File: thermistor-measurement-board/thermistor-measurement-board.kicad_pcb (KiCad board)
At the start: 4 copper layers, 50.8 x 30.5 mm, 94 parts, among them P201 BIAS, P301 MEASURE, P401 PWR, P402 BIAS, P403 OUT_A, P404 OUT_B, P406 I/O, U201 MAX14661, U202 AD8607, U203 AD8277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

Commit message: some schematic review and a new TODO list
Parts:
- R301, R302: value R -> 660k
- R311, R312: value 0 -> 100k
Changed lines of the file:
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@@
     (links 287)
     (no_connects 0)
-    (area 156.794287 61.92 221.680798 101.93528)
+    (area 168.834999 69.774999 219.785001 100.405001)
     (thickness 1.6)
     (drawings 16)
@@
       (effects (font (size 0.508 0.508) (thickness 0.0762)))
     )
-    (fp_text value R (at 0 0.097102 270) (layer F.Fab)
+    (fp_text value 660k (at 0 0.097102 270) (layer F.Fab)
       (effects (font (size 0.508 0.508) (thickness 0.0762)))
     )
@@
       (effects (font (size 0.508 0.508) (thickness 0.0762)))
     )
-    (fp_text value R (at 0 0.097102 270) (layer F.Fab)
+    (fp_text value 660k (at 0 0.097102 270) (layer F.Fab)
       (effects (font (size 0.508 0.508) (thickness 0.0762)))
     )
@@
       (effects (font (size 0.508 0.508) (thickness 0.0762)))
     )
-    (fp_text value 0 (at 0 0.032742) (layer F.Fab)
+    (fp_text value 100k (at 0 0.032742) (layer F.Fab)
       (effects (font (size 0.508 0.508) (thickness 0.0762)))
     )
@@
       (effects (font (size 0.508 0.508) (thickness 0.0762)))
     )
-    (fp_text value 0 (at 0 0.179742) (layer F.Fab)
-      (effects (font (size 0.508 0.508) (thickness 0.0762)))
-    )
+    (fp_text value 100k (at 0 0.179742) (layer F.Fab)
+      (effects (font (size 0.508 0.508) (thickness 0.0762)))
+    )

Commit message: took care of a few board review tasks
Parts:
- added C322: 0.1u, Capacitors_SMD:C_0402, F.Cu at (188.8, 85.8)
- added P405: ADC_REF, Pin_Headers:Pin_Header_Straight_1x02, F.Cu at (175.3, 71.1)
- added R211: 100k, Resistors_SMD:R_0402, F.Cu at (216.1, 91.9)
- added R212: 100k, Resistors_SMD:R_0402, F.Cu at (210.4, 91.8)
- added R324: 0, Resistors_SMD:R_0603, F.Cu at (189.1, 87.4)
- R301, R302: value 660k -> 6.6M
- R311, R312: value 100k -> 1M
- moved C317 1.37 mm to (188.0, 87.1), turned to 270 degrees
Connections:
- net Net-(C317-Pad1) renamed /Interface/ADC_REF+
- U304 pad 3: /Interface/OUT_B+ -> /Interface/OUT_B-
- U304 pad 4: /Interface/OUT_B- -> /Interface/OUT_B+
- U304 pad 7: GNDA -> /Interface/ADC_REF-
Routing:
- net /Interface/ADC_REF-: track 0.00 -> 25.8 mm, vias 0 -> 1
- net /Interface/ADC_REF+: track 1.56 -> 23.4 mm, vias 0 -> 1
- net /Bias/VREF2_EN: track 13.4 -> 20.5 mm
- net GNDA: track 110.6 -> 114.5 mm, vias 43 -> 46
- net /Bias/VREF1_EN: track 10.7 -> 11.4 mm
- net GND: track 40.7 -> 40.0 mm
- net /Bias/AVCC: track 36.2 -> 36.4 mm, vias 18 -> 17
- net /Interface/OUT_B+: vias 1 -> 3
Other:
- rule trace_min: 0.127 -> 0.1524

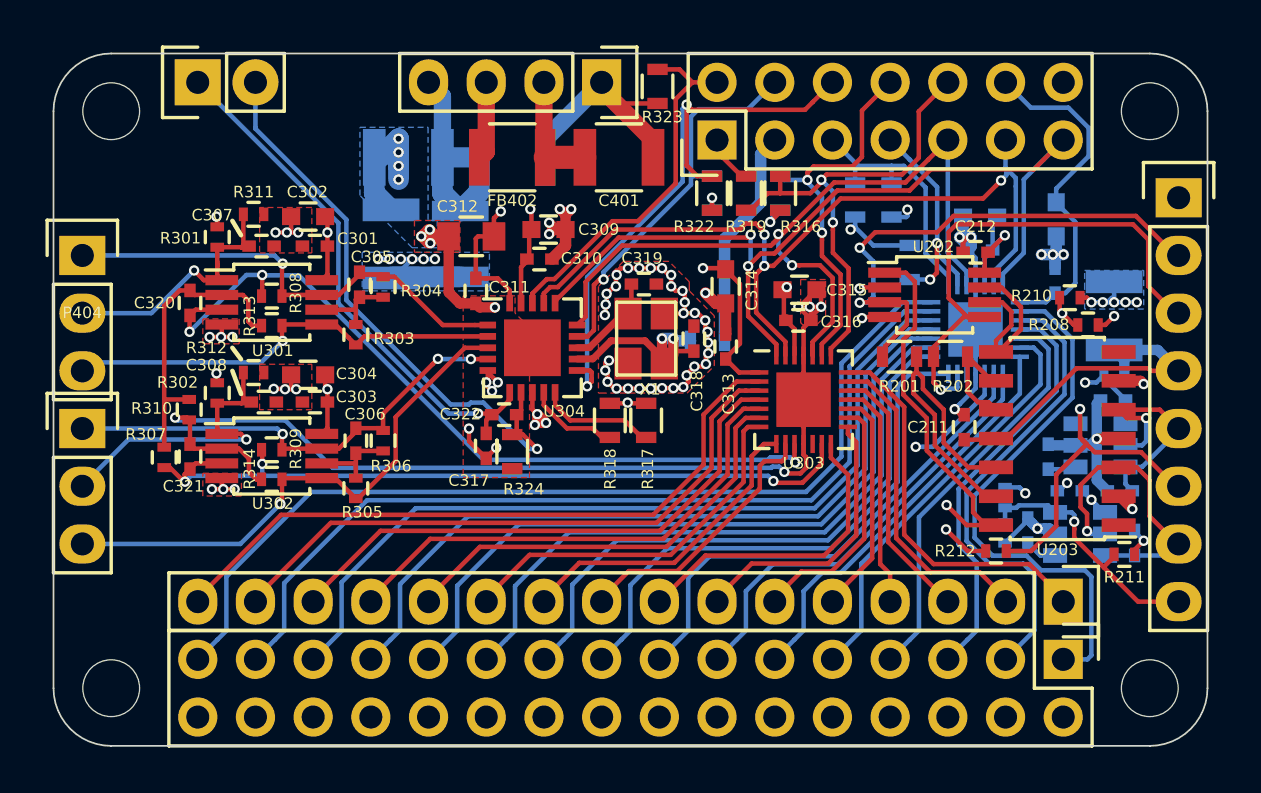
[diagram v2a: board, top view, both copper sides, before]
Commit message: reviewed footprints
they were all more or less correct, but i massaged a couple to closer match Maxim's recommended land patterns
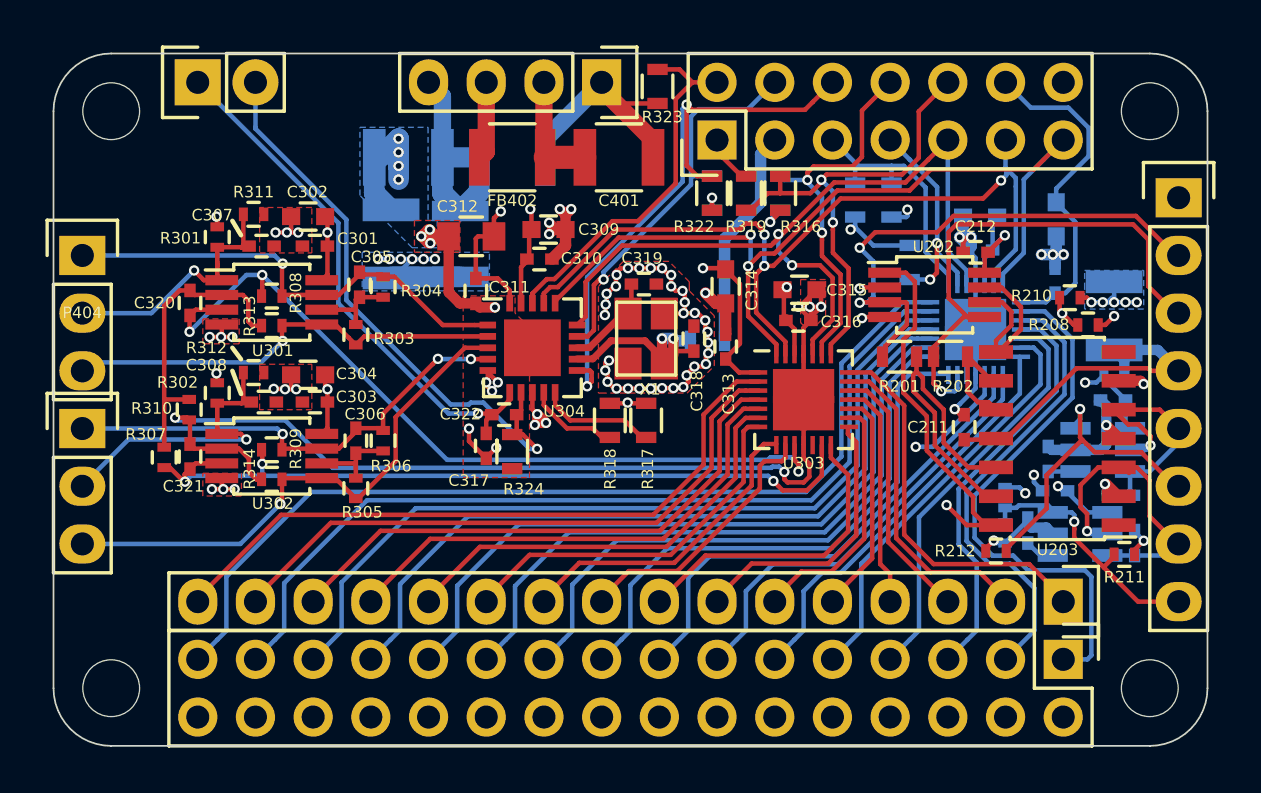
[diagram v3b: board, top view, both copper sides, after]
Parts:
- U201, U303: footprint Housings_DFN_QFN:QFN-28-1EP_4x4mm_Pitch0.4mm -> project:Maxim_90-0035
- U204, U205: footprint TO_SOT_Packages_SMD:SOT-23-6 -> project:Maxim_90-0175
- moved C207 0.65 mm to (213.0, 89.1)
- moved U205 0.22 mm to (215.1, 87.3)
- moved C206 0.21 mm to (215.9, 89.3)
- moved C210 0.10 mm to (212.7, 87.7)
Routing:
- net /Bias/AVCC: track 36.4 -> 37.8 mm
- net /Measurement/COM_A: track 35.3 -> 36.2 mm
- net /Bias/VREF2_EN: track 20.5 -> 19.7 mm
- net /Measurement/COM_B: track 34.0 -> 34.6 mm
- net GNDA: track 114.5 -> 113.9 mm, vias 46 -> 45
- net /Bias/SCLK: track 35.7 -> 35.2 mm

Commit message: some notes and minor fiddling around
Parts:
- R201, R202: value R -> 0.01%
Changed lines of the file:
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@@
     (links 296)
     (no_connects 0)
-    (area 168.871899 69.811899 219.748101 100.368101)
+    (area 156.794287 61.92 221.680798 101.93528)
     (thickness 1.6)
     (drawings 15)
@@
       (effects (font (size 0.508 0.508) (thickness 0.0762)))
     )
-    (fp_text value R (at -0.058 -0.036 180) (layer F.Fab)
+    (fp_text value 0.01% (at -0.058 -0.036 180) (layer F.Fab)
       (effects (font (size 0.508 0.508) (thickness 0.0762)))
     )
@@
       (effects (font (size 0.508 0.508) (thickness 0.0762)))
     )
-    (fp_text value R (at 0 -0.012 180) (layer F.Fab)
-      (effects (font (size 0.508 0.508) (thickness 0.0762)))
-    )
+    (fp_text value 0.01% (at 0 -0.012 180) (layer F.Fab)
+      (effects (font (size 0.508 0.508) (thickness 0.0762)))
+    )

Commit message: lots of design review and related fixes/improvements
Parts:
- added C323: 100p, Capacitors_SMD:C_0402, F.Cu at (186.6, 82.3)
- added C324: 100p, Capacitors_SMD:C_0402, F.Cu at (186.6, 84.4)
- added D301: 1.8V, Diodes_SMD:SOD-123, B.Cu at (174.4, 86.4)
- added D302: 1.8V, Diodes_SMD:SOD-123, B.Cu at (174.4, 78.7)
- added D303: 1.8V, Diodes_SMD:SOD-123, B.Cu at (174.4, 91.4)
- added D304: 1.8V, Diodes_SMD:SOD-123, B.Cu at (174.4, 83.8)
- added R325: 0, Resistors_SMD:R_0603, F.Cu at (185.0, 86.1)
- added R326: 0, Resistors_SMD:R_0603, F.Cu at (185.6, 84.4)
- C322: value 0.1u -> 100p
- P405: footprint Pin_Headers:Pin_Header_Straight_1x02 -> Pin_Headers:Pin_Header_Straight_1x04
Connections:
- P405 pad 2: /Interface/ADC_REF- -> /Interface/ADC_REF+
- U304 pad 3: /Interface/OUT_B- -> Net-(C324-Pad1)
- U304 pad 4: /Interface/OUT_B+ -> Net-(C324-Pad2)
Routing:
- net /Interface/ADC_REF+: track 23.4 -> 50.0 mm, vias 1 -> 2
- net /Interface/ADC_REF-: track 25.8 -> 46.9 mm, vias 1 -> 2
- net /Interface/OUT_B+: track 21.1 -> 16.6 mm, vias 3 -> 1
- net Net-(C324-Pad2): track 0.00 -> 4.01 mm
- net /Interface/OUT_B-: track 23.9 -> 20.1 mm
- net Net-(C324-Pad1): track 0.00 -> 2.94 mm
- net GNDA: track 113.9 -> 115.3 mm, vias 45 -> 47
- net /Interface/OUT_A+: track 20.9 -> 21.7 mm
- net /Measurement/COM_A: track 36.2 -> 36.9 mm

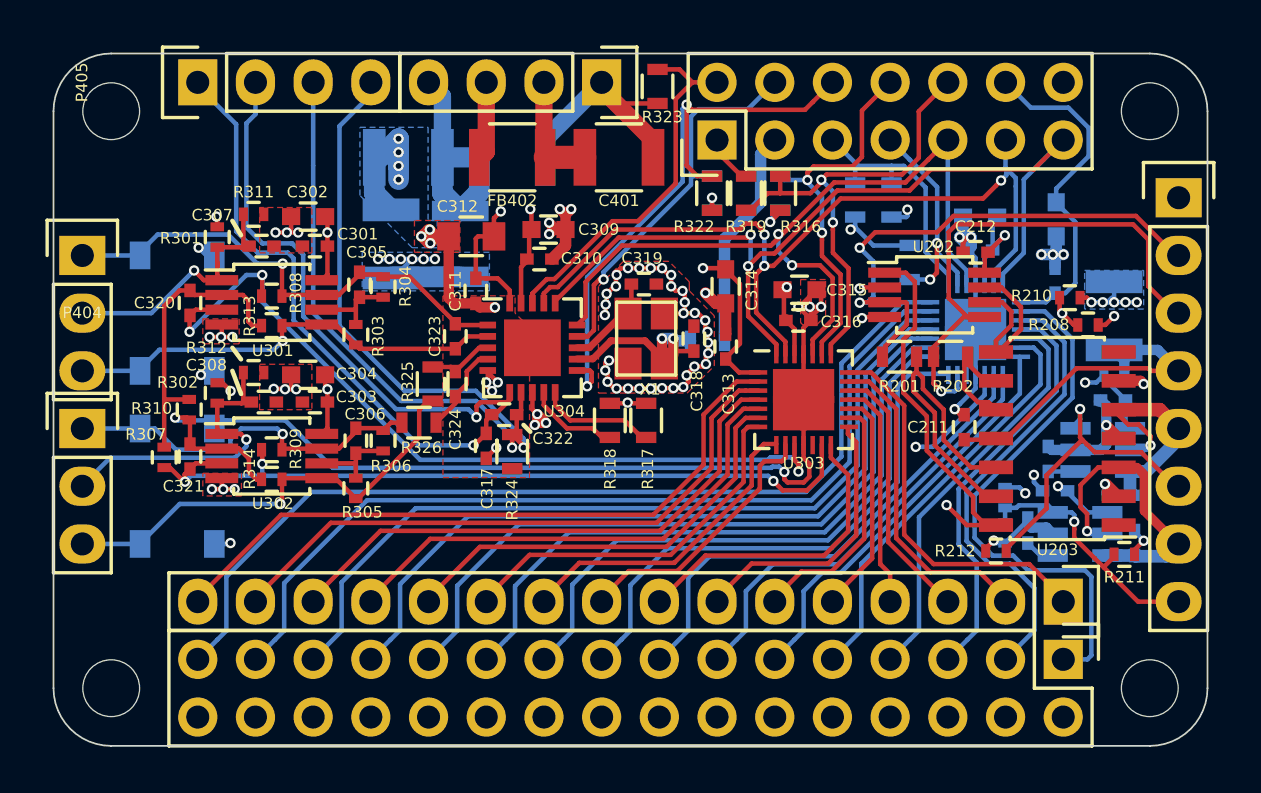
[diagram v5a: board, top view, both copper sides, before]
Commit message: read a million instrument amp datasheets and found one that should work nicely for low gain.
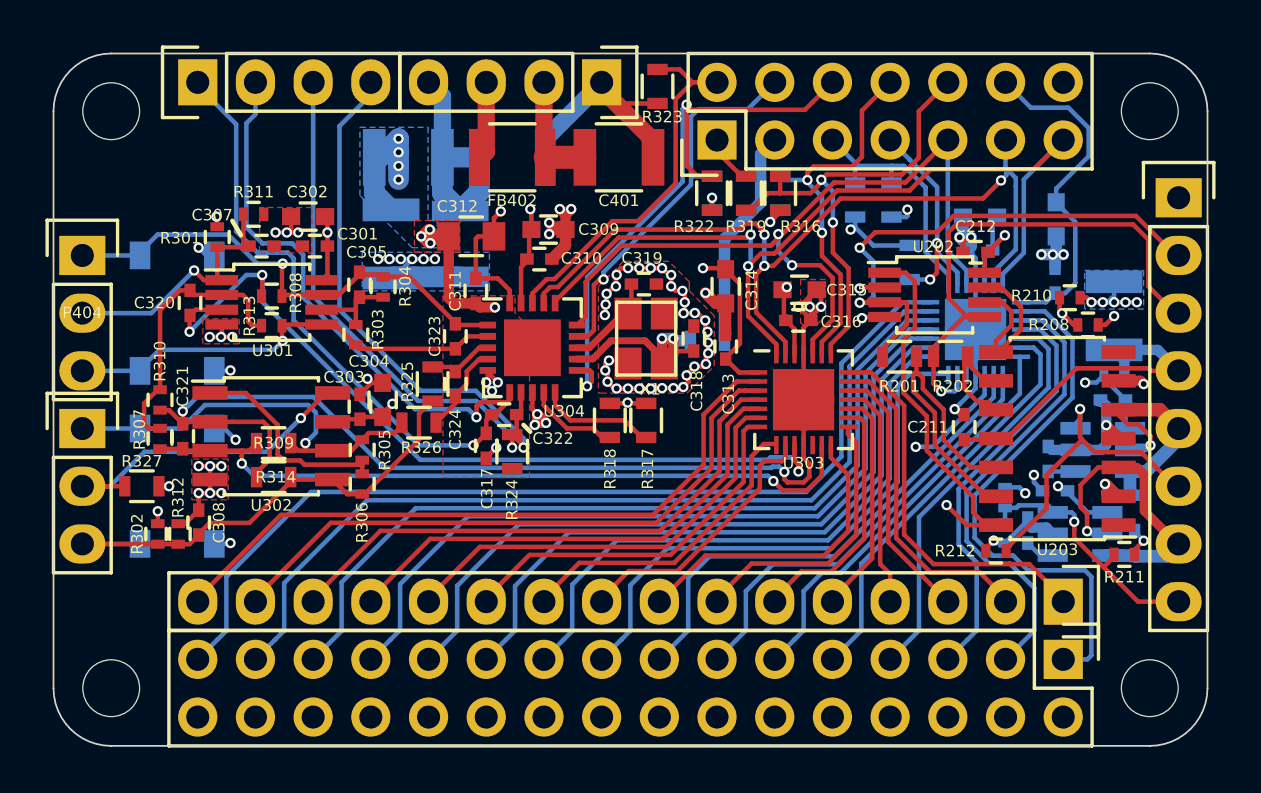
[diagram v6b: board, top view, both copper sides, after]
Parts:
- removed C306: 0.01u, Capacitors_SMD:C_0402
- removed REF** (x4): MountingHole_2-5mm, Mounting_Holes:MountingHole_2-5mm
- added H401: MountingHole, MountingHole_2-5mm, F.Cu at (171.4, 72.4)
- added H402: MountingHole, MountingHole_2-5mm, F.Cu at (217.2, 72.4)
- added H403: MountingHole, MountingHole_2-5mm, F.Cu at (171.4, 97.8)
- added H404: MountingHole, MountingHole_2-5mm, F.Cu at (217.2, 97.8)
- added R327: 100k, Resistors_SMD:R_0603, F.Cu at (172.8, 88.9)
- R301, R302: value 6.6M -> 7.5M
- R304: value 0 -> 63k
- R305: value 1k -> 0
- R306: value 99k -> ∞
- R309, R314: footprint Resistors_SMD:R_0402 -> Resistors_SMD:R_0603
- R311, R312: value 1M -> 2.5M
- U301: value MAX4208 -> MAX4209
- U302: value MAX4209 -> MCP6N11; footprint Housings_SSOP:MSOP-8_3x3mm_Pitch0.65mm -> Housings_SOIC:SOIC-8_3.9x4.9mm_Pitch1.27mm
- moved R312 7.84 mm to (174.4, 91.0), turned to 90 degrees
- moved R302 6.74 mm to (173.5, 91.0)
- moved C308 6.03 mm to (175.3, 90.5), turned to 90 degrees
- moved C304 3.46 mm to (183.4, 85.1), turned to 90 degrees
- moved R306 2.12 mm to (182.5, 88.8), turned to 270 degrees
- moved C303 1.99 mm to (182.4, 85.4), turned to 90 degrees
- moved R305 1.72 mm to (182.5, 87.3), turned to 90 degrees
- moved R310 1.35 mm to (173.6, 85.1)
- moved C321 0.95 mm to (174.6, 86.7)
- moved U302 0.87 mm to (178.5, 86.7)
- moved R307 0.85 mm to (173.6, 86.8)
- moved R309 0.31 mm to (178.6, 87.0)
- moved R314 0.12 mm to (178.6, 88.5)
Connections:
- net /Bias/DVDD renamed /ADC/DVDD
- net /Bias/MISO renamed /ADC/MISO
- net /Bias/MOSI renamed /ADC/MOSI
- net /Bias/SCLK renamed /ADC/SCLK
- net /Interface/ADC_CS renamed /ADC/ADC_CS
- net /Interface/ADC_DR_INT renamed /ADC/ADC_DR_INT
- net /Interface/ADC_MCLK renamed /ADC/ADC_MCLK
- net /Interface/ADC_REF+ renamed /ADC/ADC_REF+
- net /Interface/ADC_REF- renamed /ADC/ADC_REF-
- net /Interface/ADC_RST renamed /ADC/ADC_RST
- net /Interface/OUT_A+ renamed /ADC/OUT_A+
- net /Interface/OUT_A- renamed /ADC/OUT_A-
- net /Measurement/ADC_OSC1 renamed /ADC/ADC_OSC1
- net /Measurement/ADC_OSC2 renamed /ADC/ADC_OSC2
- net /Measurement/COM_A renamed /Sensor input/COM_A
- net /Measurement/COM_B renamed /Sensor input/COM_B
- net Net-(C320-Pad2) renamed /Sensor input/IN_A-
- C201 pad 1: /Bias/AVCC -> /ADC/AVCC
- C202 pad 1: /Bias/AVCC -> /ADC/AVCC
- C207 pad 1: /Bias/AVCC -> /ADC/AVCC
- C209 pad 1: /Bias/AVCC -> /ADC/AVCC
- C212 pad 1: /Bias/AVCC -> /ADC/AVCC
- C301 pad 1: /Bias/AVCC -> /ADC/AVCC
- C302 pad 1: /Bias/AVCC -> /ADC/AVCC
- C303 pad 1: /Bias/AVCC -> /ADC/AVCC
- C304 pad 1: /Bias/AVCC -> /ADC/AVCC
- C308 pad 1: /Interface/REF_B -> /ADC/OUT_B-
- C311 pad 1: /Bias/AVCC -> /ADC/AVCC
- C312 pad 1: /Bias/AVCC -> /ADC/AVCC
- C315 pad 1: /Bias/AVCC -> /ADC/AVCC
- C316 pad 1: /Bias/AVCC -> /ADC/AVCC
- C403 pad 1: /Bias/AVCC -> /ADC/AVCC
- D301 pad 1: /Interface/OUT_B+ -> /ADC/OUT_B+
- D303 pad 1: /Interface/OUT_B- -> /ADC/OUT_B-
- P404 pad 1: /Interface/OUT_B+ -> /ADC/OUT_B+
- P404 pad 2: /Interface/REF_B -> /Sensor input/AMP_B_EN
- P404 pad 3: /Interface/OUT_B- -> /ADC/OUT_B-
- R206 pad 2: /Bias/AVCC -> /ADC/AVCC
- R207 pad 2: /Bias/AVCC -> /ADC/AVCC
- R208 pad 2: /Bias/AVCC -> /ADC/AVCC
- R301 pad 1: /Bias/AVCC -> /ADC/AVCC
- R302 pad 1: /Bias/AVCC -> /ADC/AVCC
- R302 pad 2: /Interface/REF_B -> /ADC/OUT_B-
- R305 pad 1: Net-(C306-Pad1) -> Net-(R305-Pad1)
- R305 pad 2: /Interface/OUT_B- -> /ADC/OUT_B+
- R306 pad 1: Net-(C306-Pad1) -> Net-(R305-Pad1)
- R306 pad 2: /Interface/OUT_B+ -> /ADC/OUT_B-
- R309 pad 2: /Interface/OUT_B+ -> /ADC/OUT_B+
- R312 pad 1: /Interface/REF_B -> /ADC/OUT_B-
- R314 pad 2: /Interface/OUT_B- -> /ADC/OUT_B-
- R325 pad 1: /Interface/OUT_B+ -> /ADC/OUT_B+
- R326 pad 1: /Interface/OUT_B- -> /ADC/OUT_B-
- R401 pad 1: /Bias/AVCC -> /ADC/AVCC
- U201 pad 26: /Bias/AVCC -> /ADC/AVCC
- U202 pad 8: /Bias/AVCC -> /ADC/AVCC
- U204 pad 4: /Bias/AVCC -> /ADC/AVCC
- U205 pad 4: /Bias/AVCC -> /ADC/AVCC
- U301 pad 8: /Bias/AVCC -> /ADC/AVCC
- U302 pad 1: /Interface/REF_B -> Net-(R305-Pad1)
- U302 pad 5: /Interface/OUT_B- -> /ADC/OUT_B-
- U302 pad 6: Net-(C306-Pad1) -> /ADC/OUT_B+
- U302 pad 7: /Interface/OUT_B+ -> /ADC/AVCC
- U302 pad 8: /Bias/AVCC -> /Sensor input/AMP_B_EN
- U303 pad 26: /Bias/AVCC -> /ADC/AVCC
- U304 pad 20: /Bias/AVCC -> /ADC/AVCC
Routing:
- net /ADC/AVCC: track 0.00 -> 38.2 mm, vias 0 -> 17
- net /Bias/AVCC: track 38.1 -> 0.00 mm, vias 17 -> 0
- net /ADC/OUT_B-: track 0.00 -> 22.3 mm
- net /Interface/OUT_B-: track 20.1 -> 0.00 mm, vias 1 -> 0
- net /ADC/OUT_B+: track 0.00 -> 18.3 mm, vias 0 -> 1
- net /Interface/OUT_B+: track 16.6 -> 0.00 mm, vias 1 -> 0
- net /Sensor input/AMP_B_EN: track 0.00 -> 14.6 mm, vias 0 -> 1
- net /Interface/REF_B: track 13.8 -> 0.00 mm, vias 1 -> 0
- net Net-(R305-Pad1): track 0.00 -> 9.39 mm
- net GNDA: track 115.3 -> 122.0 mm, vias 47 -> 50
- net Net-(C306-Pad1): track 3.86 -> 0.00 mm
- net /Sensor input/COM_B: track 34.6 -> 32.7 mm, vias 3 -> 2
- net /Sensor input/IN_A-: track 13.1 -> 12.1 mm
- net /ADC/ADC_REF-: track 46.9 -> 46.0 mm
- added copper zone on In1.Cu, net (none)
- added copper zone on B.Cu, net /ADC/AVCC
- added copper zone on In2.Cu, net /ADC/AVCC
- removed copper zone on B.Cu, net /Bias/AVCC
- removed copper zone on In2.Cu, net /Bias/AVCC

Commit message: a few minor tweaks to thermistor board
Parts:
- added R501: 0, Resistors_SMD:R_0603, F.Cu at (184.9, 81.6)
- added R502: 0, Resistors_SMD:R_0603, F.Cu at (184.9, 82.9)
- R327: value 100k -> 1M
- moved R325 1.90 mm to (185.0, 88.0)
- moved R326 1.80 mm to (185.6, 86.2)
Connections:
- C323 pad 1: /ADC/OUT_A- -> Net-(C323-Pad1)
- C323 pad 2: /ADC/OUT_A+ -> Net-(C323-Pad2)
- U304 pad 1: /ADC/OUT_A+ -> Net-(C323-Pad2)
- U304 pad 2: /ADC/OUT_A- -> Net-(C323-Pad1)
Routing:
- net /ADC/OUT_A-: track 19.9 -> 16.1 mm
- net /ADC/OUT_A+: track 21.7 -> 18.3 mm
- net Net-(C323-Pad1): track 0.00 -> 2.62 mm
- net Net-(C323-Pad2): track 0.00 -> 2.51 mm
- net Net-(C324-Pad2): track 4.01 -> 6.18 mm
- net Net-(C324-Pad1): track 2.94 -> 3.87 mm
- net /ADC/OUT_B-: track 22.3 -> 21.6 mm
